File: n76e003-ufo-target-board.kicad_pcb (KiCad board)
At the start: 2 copper layers, 52.3 x 68.1 mm, 10 parts, among them J1 CW308T_CONNBOARD, U2 N76E003AT20

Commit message: switch gpio1 and gpio2 lines, update gerbers, notes
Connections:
- J1 pad B17: GPI02 -> GPI01
- J1 pad B19: GPI01 -> GPI02
- U2 pad 2: GPI02 -> GPI01
- U2 pad 3: GPI01 -> GPI02
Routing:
- net GPI02: track 73.4 -> 77.3 mm
- net GPI01: track 76.6 -> 73.4 mm
- net GND: vias 55 -> 57
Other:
- board text added: "v1.2"
- board text removed: "v1.1"

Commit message: add C2 footprint back, exclude from BOM by default
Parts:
- added C2: 2.2uF, Capacitor_SMD:C_0805_2012Metric_Pad1.18x1.45mm_HandSolder, F.Cu at (156.3, 83.0)
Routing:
- net Net-(J1-FILT_LP): track 25.2 -> 28.9 mm
- net GND: vias 57 -> 58
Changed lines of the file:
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@@
     (pad "20" smd roundrect (at 2.865 -2.925) (size 1.48 0.41) (layers "F.Cu" "F.Paste" "F.Mask") (roundrect_rratio 0.02)
       (net 9 "GPI04") (pinfunction "P0.4/AIN5/STADC/PWM3/IC3") (pintype "bidirectional"))
+    (model "${KICAD7_3DMODEL_DIR}/Package_SO.3dshapes/SSOP-20_4.4x6.5mm_P0.65mm.wrl"
+      (offset (xyz 0 0 0))
+      (scale (xyz 1 1 1))
+      (rotate (xyz 0 0 0))
+    )
+  )
+  (footprint "Capacitor_SMD:C_0805_2012Metric_Pad1.18x1.45mm_HandSolder" (layer "F.Cu")
+    (at 156.325 83 -90)
+    (descr "Capacitor SMD 0805 (2012 Metric), square (rectangular) end terminal, IPC_7351 nominal with elongated pad for handsoldering. (Body size source: IPC-SM-782 page 76, https://www.pcb-3d.com/wordpress/wp-content/uploads/ipc-sm-782a_amendment_1_and_2.pdf, https://docs.google.com/spreadsheets/d/1BsfQQcO9C6DZCsRaXUlFlo91Tg2WpOkGARC1WS5S8t0/edit?usp=sharing), generated with kicad-footprint-generator")
+    (tags "capacitor handsolder")
+    (property "Sheetfile" "n76e003-ufo-target-board.kicad_sch")
+    (property "Sheetname" "")
+    (property "ki_description" "Unpolarized capacitor, small symbol")
+    (property "ki_keywords" "capacitor cap")
+    (attr smd exclude_from_pos_files exclude_from_bom)
+    (fp_text reference "C2" (at 0 1.8 -90) (layer "F.SilkS")
+        (effects (font (size 1 1) (thickness 0.15)))
+    )
+    (fp_text value "2.2uF" (at 0 1.68 -90) (layer "F.Fab")
+        (effects (font (size 1 1) (thickness 0.15)))
+    )
+    (fp_text user "${REFERENCE}" (at 0 0 -90) (layer "F.Fab")
+        (effects (font (size 0.5 0.5) (thickness 0.08)))
+    )
+    (fp_line (start -0.261252 -0.735) (end 0.261252 -0.735)
+      (stroke (width 0.12) (type solid)) (layer "F.SilkS"))
+    (fp_line (start -0.261252 0.735) (end 0.261252 0.735)
+      (stroke (width 0.12) (type solid)) (layer "F.SilkS"))
+    (fp_line (start -1.88 -0.98) (end 1.88 -0.98)
+      (stroke (width 0.05) (type solid)) (layer "F.CrtYd"))
+    (fp_line (start -1.88 0.98) (end -1.88 -0.98)
+      (stroke (width 0.05) (type solid)) (layer "F.CrtYd"))
+    (fp_line (start 1.88 -0.98) (end 1.88 0.98)
+      (stroke (width 0.05) (type solid)) (layer "F.CrtYd"))
+    (fp_line (start 1.88 0.98) (end -1.88 0.98)
+      (stroke (width 0.05) (type solid)) (layer "F.CrtYd"))
+    (fp_line (start -1 -0.625) (end 1 -0.625)
+      (stroke (width 0.1) (type solid)) (layer "F.Fab"))
+    (fp_line (start -1 0.625) (end -1 -0.625)
+      (stroke (width 0.1) (type solid)) (layer "F.Fab"))
+    (fp_line (start 1 -0.625) (end 1 0.625)
+      (stroke (width 0.1) (type solid)) (layer "F.Fab"))
+    (fp_line (start 1 0.625) (end -1 0.625)
+      (stroke (width 0.1) (type solid)) (layer "F.Fab"))
+    (pad "1" smd roundrect (at -1.0375 0 270) (size 1.175 1.45) (layers "F.Cu" "F.Paste" "F.Mask") (roundrect_rratio 0.2127659574)
+      (net 3 "Net-(J1-FILT_LP)") (pintype "passive"))
+    (pad "2" smd roundrect (at 1.0375 0 270) (size 1.175 1.45) (layers "F.Cu" "F.Paste" "F.Mask") (roundrect_rratio 0.2127659574)
+      (net 2 "GND") (pintype "passive"))
+    (model "${KICAD6_3DMODEL_DIR}/Capacitor_SMD.3dshapes/C_0805_2012Metric.wrl"
+      (offset (xyz 0 0 0))
+      (scale (xyz 1 1 1))
+      (rotate (xyz 0 0 0))
+    )
   )
   (footprint "Jumper:SolderJumper-2_P1.3mm_Open_RoundedPad1.0x1.5mm" (layer "F.Cu")
@@
   (via (at 151.97 76.75) (size 0.635) (drill 0.3048) (layers "F.Cu" "B.Cu") (net 2))
   (via (at 128.61 83.4) (size 0.635) (drill 0.3048) (layers "F.Cu" "B.Cu") (net 2))
+  (via (at 156.325 85.8375) (size 1.27) (drill 0.7112) (layers "F.Cu" "B.Cu") (free) (net 2))
   (via (at 166.85 99.6) (size 0.635) (drill 0.3048) (layers "F.Cu" "B.Cu") (net 2))
   (via (at 146.25 80.95) (size 0.635) (drill 0.3048) (layers "F.Cu" "B.Cu") (free) (net 2))
@@
   (segment (start 163.1025 81.965) (end 163.1025 83.9025) (width 0.508) (layer "F.Cu") (net 3))
   (segment (start 163.1025 83.9025) (end 164.8 85.6) (width 0.508) (layer "F.Cu") (net 3))
+  (segment (start 156.325 81.9625) (end 160.02 81.9625) (width 0.508) (layer "F.Cu") (net 3))
   (segment (start 172.8395 80.9042) (end 169.7858 80.9042) (width 0.508) (layer "F.Cu") (net 3))
   (segment (start 168.64 82.05) (end 163.1875 82.05) (width 0.508) (layer "F.Cu") (net 3))

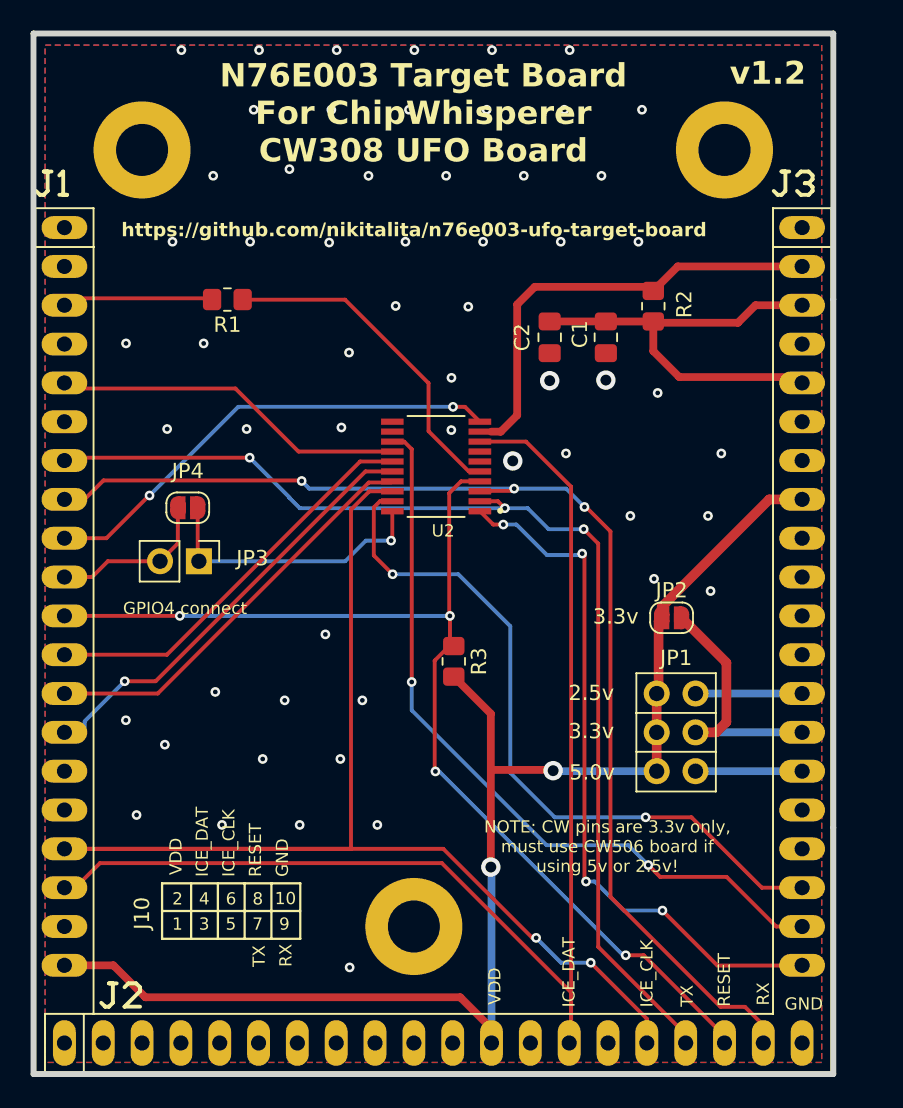
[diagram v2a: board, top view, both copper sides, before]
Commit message: v1.3
Remove GPIO4 connect header, bump shunt resistor value to 51R, update on-board notes
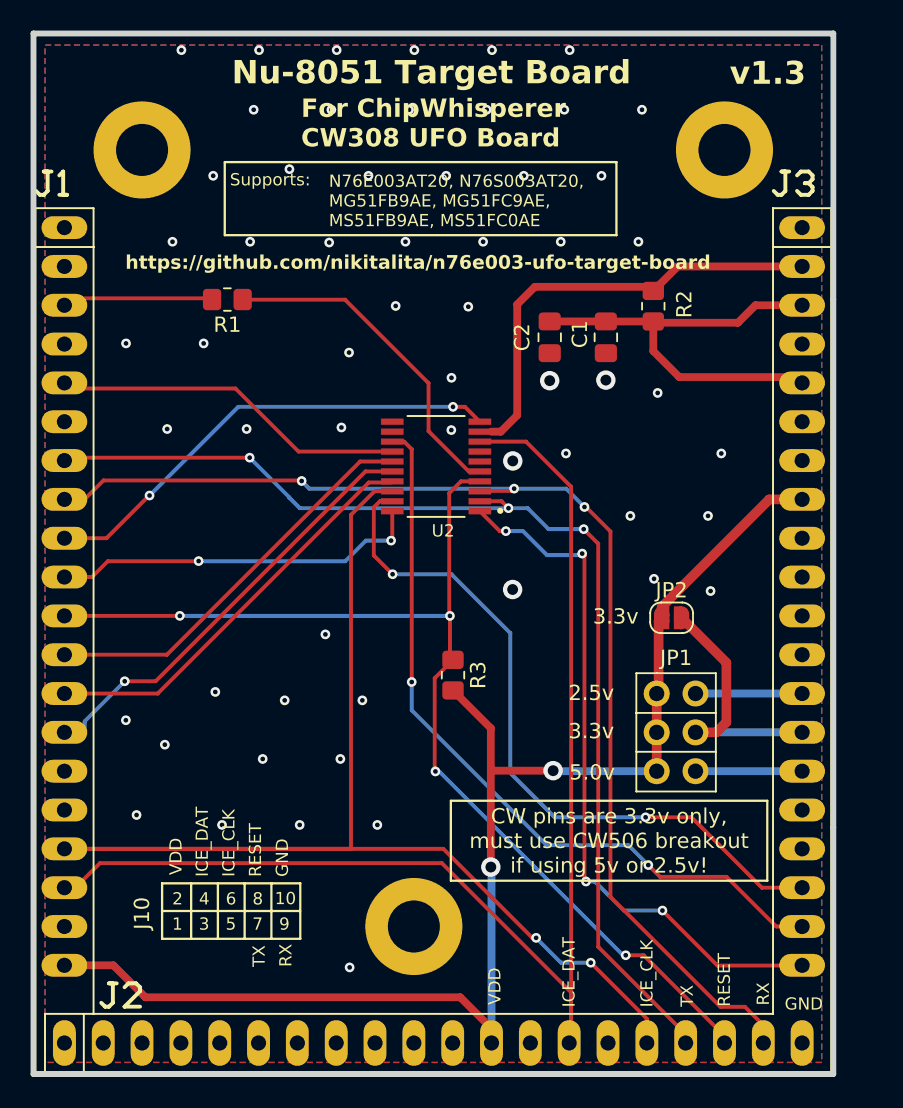
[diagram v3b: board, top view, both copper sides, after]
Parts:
- removed JP3: GPIO4_connect, Connector_PinHeader_2.54mm:PinHeader_1x02_P2.54mm_Vertical
- removed JP4: GPIO4_connect, Jumper:SolderJumper-2_P1.3mm_Open_RoundedPad1.0x1.5mm
- C2: value 2.2uF -> 2.2uF (OPT)
- R2: value 22R -> 51R
- moved R3 0.90 mm to (150.0, 105.1), turned to 90 degrees
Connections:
- J1 pad A10: Net-(J1-GPIO4) -> GPI04
- R3 pad 1: RST -> VCC
- R3 pad 2: VCC -> RST
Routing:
- net Net-(J1-GPIO4): track 10.6 -> 0.00 mm
- net GPI04: track 18.0 -> 24.3 mm, vias 1 -> 2
- net VCC: track 88.3 -> 87.4 mm
- net GND: vias 58 -> 59
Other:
- board text added: "CW pins are 3.3v only, must use CW506 breakout if using 5v or 2.5v!"
- board text added: "For ChipWhisperer CW308 UFO Board"
- board text added: "N76E003AT20, N76S003AT20, MG51FB9AE, MG51FC9AE, MS51FB9AE, MS51FC0AE"
- board text added: "Nu-8051 Target Board"
- board text added: "Supports:"
- board text added: "v1.3"
- board text removed: "GPIO4 connect"
- board text removed: "N76E003 Target Board For ChipWhisperer CW308 UFO Board"
- board text removed: "NOTE: CW pins are 3.3v only, must use CW506 board if using 5v or 2.5v!"
- board text removed: "v1.2"
